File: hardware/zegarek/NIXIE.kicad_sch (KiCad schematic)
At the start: 32 parts, among them U6 74141, U7 74141, U8 74141, U9 74141

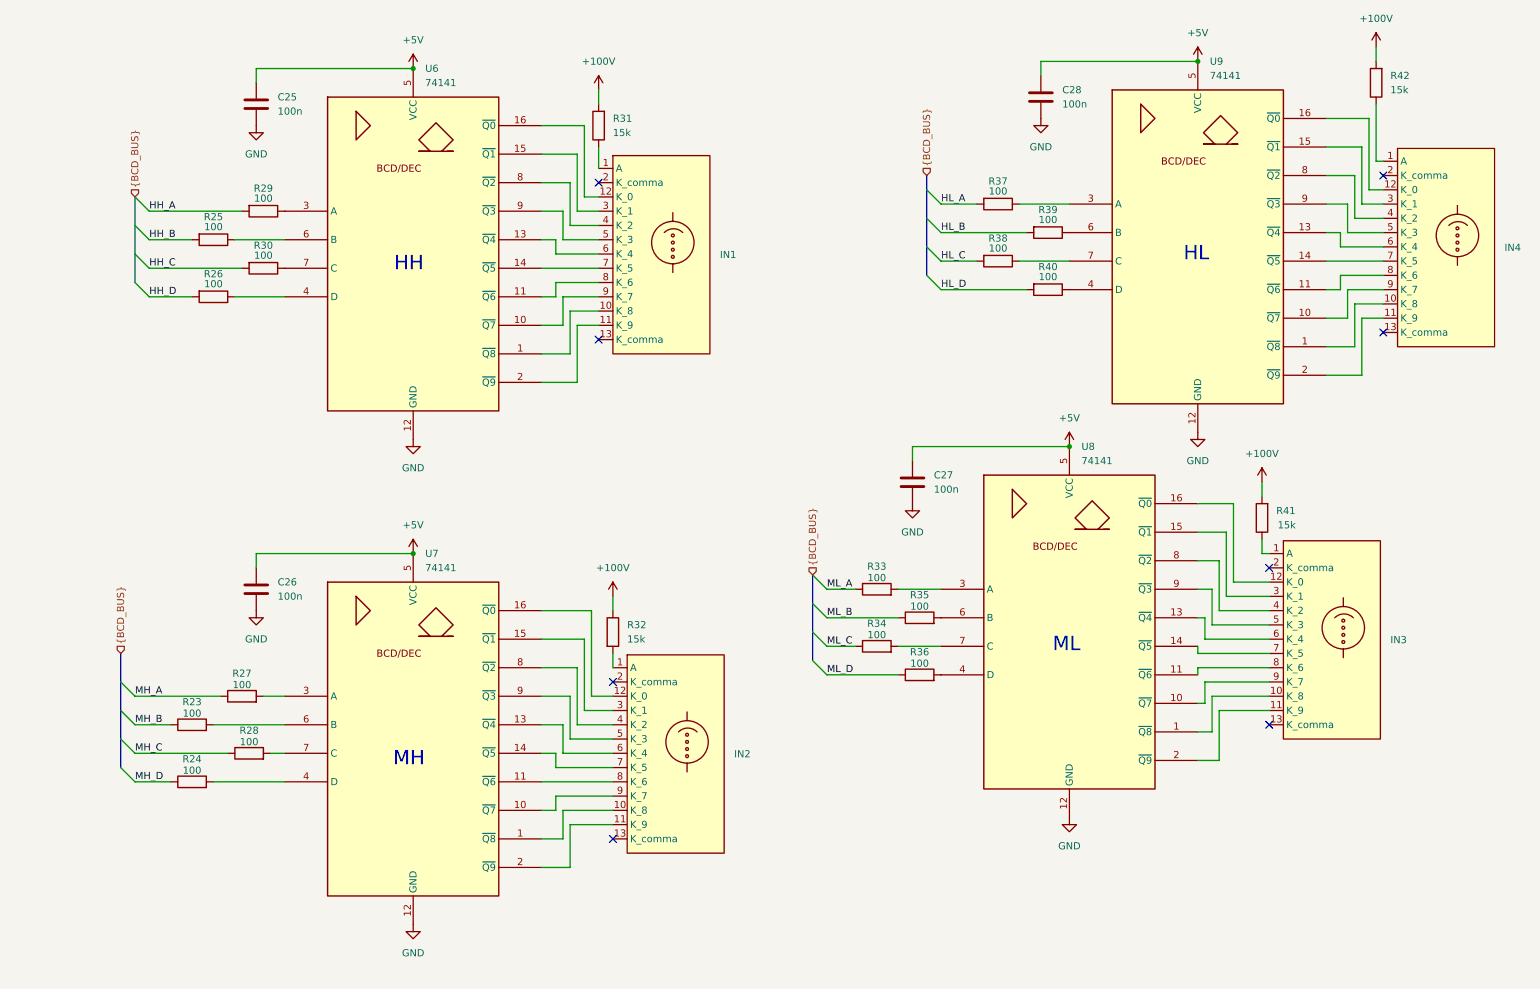
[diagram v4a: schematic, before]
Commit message: new revision with fixes from prototype: level shift to mcu added, changed con footprints and debug usb deleted
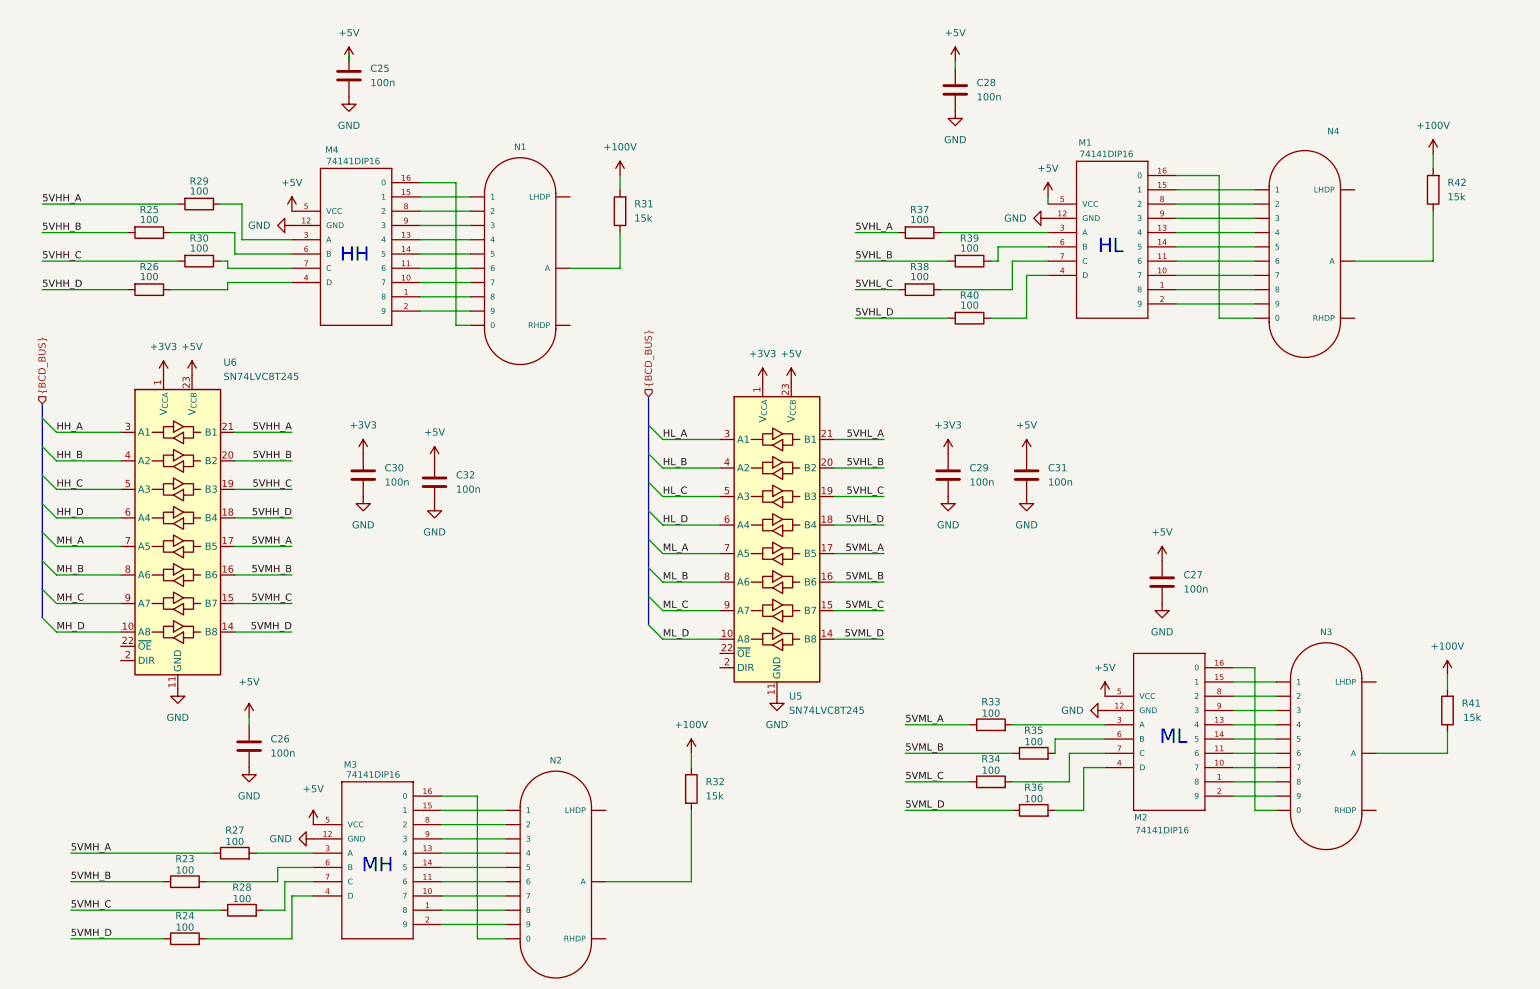
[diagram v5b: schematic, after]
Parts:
- removed IN1, IN2, IN3, IN4: (no value), Relay_THT:IN-14 NIXIE TUBE, symbol New_Library:IN-14
- removed U6, U7, U8, U9: 74141, Package_DIP:CERDIP-16_W7.62mm_SideBrazed_LongPads, symbol 74xx_IEEE:74141
- added C29, C30, C31, C32: 100n, Capacitor_SMD:C_1206_3216Metric_Pad1.33x1.80mm_HandSolder, symbol Device:C
- added M1, M2, M3, M4: 74141DIP16, nixiemisc:nixiemisc-DIP16, symbol nixiemisc:74141DIP16
- added N1, N2, N3, N4: IN-14, nixies-us:nixies-us-IN-14, symbol nixies-us:IN-14
- added U5, U6: SN74LVC8T245, Package_SO:SSOP-24_3.9x8.7mm_P0.635mm, symbol Logic_LevelTranslator:SN74LVC8T245
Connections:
- net +5V: now also C31.1, C32.1, M1.5 (VCC), M2.5 (VCC), M3.5 (VCC), M4.5 (VCC), U5.23 (V_{CCB}), U5.24 (V_{CCB}), U6.23 (V_{CCB}), U6.24 (V_{CCB})
- net GND: now also C29.2, C30.2, C31.2, C32.2, M1.12 (GND), M2.12 (GND), M3.12 (GND), M4.12 (GND), U5.11 (GND), U5.12 (GND), U5.13 (GND), U6.11 (GND), U6.12 (GND), U6.13 (GND)
- net HH_A: now also U6.3 (A1); no longer R29.2
- net HH_B: now also U6.4 (A2); no longer R25.2
- net HH_C: now also U6.5 (A3); no longer R30.2
- net HH_D: now also U6.6 (A4); no longer R26.2
- net HL_A: now also U5.3 (A1); no longer R37.2
- net HL_B: now also U5.4 (A2); no longer R39.2
- net HL_C: now also U5.5 (A3); no longer R38.2
- net HL_D: now also U5.6 (A4); no longer R40.2
- net MH_A: now also U6.7 (A5); no longer R27.1
- net MH_B: now also U6.8 (A6); no longer R23.1
- net MH_C: now also U6.9 (A7); no longer R28.1
- net MH_D: now also U6.10 (A8); no longer R24.1
- net ML_A: now also U5.7 (A5); no longer R33.1
- net ML_B: now also U5.8 (A6); no longer R35.1
- net ML_C: now also U5.9 (A7); no longer R34.1
- net ML_D: now also U5.10 (A8); no longer R36.1
- net at R40.1: now also M1.4 (D)
- net at R27.2: now also M3.3 (A)
- net at R24.2: now also M3.4 (D)
- net at R23.2: now also M3.6 (B)
- net at R28.2: now also M3.7 (C)
- net at R35.2: now also M2.6 (B)
- net at R29.1: now also M4.3 (A)
- net at R33.2: now also M2.3 (A)
- net at R38.1: now also M1.7 (C)
- net at R42.1: now also N4.A
- net at R36.2: now also M2.4 (D)
- net at R30.1: now also M4.7 (C)
- net at R37.1: now also M1.3 (A)
- net at R26.1: now also M4.4 (D)
- net at R25.1: now also M4.6 (B)
- net at R41.1: now also N3.A
- net at R31.1: now also N1.A
- net at R34.2: now also M2.7 (C)
- net at R39.1: now also M1.6 (B)
- net at R32.2: now also N2.A
- new net: M2.16 (0), N3.0
- new net: M2.15 (1), N3.1
- new net: M2.8 (2), N3.2
- new net: M2.9 (3), N3.3
- new net: M2.13 (4), N3.4
- new net: M2.14 (5), N3.5
- new net: M2.11 (6), N3.6
- new net: M2.10 (7), N3.7
- new net: M2.1 (8), N3.8
- new net: M2.2 (9), N3.9
- new net: M4.1 (8), N1.8
- new net: M4.10 (7), N1.7
- new net: M4.11 (6), N1.6
- new net: M4.13 (4), N1.4
- new net: M4.14 (5), N1.5
- new net: M4.15 (1), N1.1
- new net: M4.16 (0), N1.0
- new net: M4.2 (9), N1.9
- new net: M4.8 (2), N1.2
- new net: M4.9 (3), N1.3
- new net: M3.16 (0), N2.0
- new net: M3.15 (1), N2.1
- new net: M3.8 (2), N2.2
- new net: M3.9 (3), N2.3
- new net: M3.13 (4), N2.4
- new net: M3.14 (5), N2.5
- new net: M3.11 (6), N2.6
- new net: M3.10 (7), N2.7
- new net: M3.1 (8), N2.8
- new net: M3.2 (9), N2.9
- new net: M1.16 (0), N4.0
- new net: M1.15 (1), N4.1
- new net: M1.8 (2), N4.2
- new net: M1.9 (3), N4.3
- new net: M1.13 (4), N4.4
- new net: M1.14 (5), N4.5
- new net: M1.11 (6), N4.6
- new net: M1.10 (7), N4.7
- new net: M1.1 (8), N4.8
- new net: M1.2 (9), N4.9
- new net +3V3: C29.1, C30.1, U5.1 (V_{CCA}), U6.1 (V_{CCA})
- new net 5VHH_A: R29.2, U6.21 (B1)
- new net 5VHH_B: R25.2, U6.20 (B2)
- new net 5VHH_C: R30.2, U6.19 (B3)
- new net 5VHH_D: R26.2, U6.18 (B4)
- new net 5VHL_A: R37.2, U5.21 (B1)
- new net 5VHL_B: R39.2, U5.20 (B2)
- new net 5VHL_C: R38.2, U5.19 (B3)
- new net 5VHL_D: R40.2, U5.18 (B4)
- new net 5VMH_A: R27.1, U6.17 (B5)
- new net 5VMH_B: R23.1, U6.16 (B6)
- new net 5VMH_C: R28.1, U6.15 (B7)
- new net 5VMH_D: R24.1, U6.14 (B8)
- new net 5VML_A: R33.1, U5.17 (B5)
- new net 5VML_B: R35.1, U5.16 (B6)
- new net 5VML_C: R34.1, U5.15 (B7)
- new net 5VML_D: R36.1, U5.14 (B8)
- no-connect marks 8 -> 0
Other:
- moved on the sheet: C25, C26, C27, C28, R23, R24, R25, R26, R27, R28, R29, R30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

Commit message: rerouting tubes order for proper display order
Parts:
- R40: footprint Resistor_SMD:R_1206_3216Metric_Pad1.30x1.75mm_HandSolder -> Resistor_SMD:R_0603_1608Metric_Pad0.98x0.95mm_HandSolder
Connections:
- net 5VHH_A: now also U5.21 (B1); no longer U6.21 (B1)
- net 5VHH_B: now also U5.20 (B2); no longer U6.20 (B2)
- net 5VHH_C: now also U5.19 (B3); no longer U6.19 (B3)
- net 5VHH_D: now also U5.18 (B4); no longer U6.18 (B4)
- net 5VHL_A: now also U5.17 (B5); no longer U5.21 (B1)
- net 5VHL_B: now also U5.16 (B6); no longer U5.20 (B2)
- net 5VHL_C: now also U5.15 (B7); no longer U5.19 (B3)
- net 5VHL_D: now also U5.14 (B8); no longer U5.18 (B4)
- net 5VMH_A: now also U6.21 (B1); no longer U6.17 (B5)
- net 5VMH_B: now also U6.20 (B2); no longer U6.16 (B6)
- net 5VMH_C: now also U6.19 (B3); no longer U6.15 (B7)
- net 5VMH_D: now also U6.18 (B4); no longer U6.14 (B8)
- net 5VML_A: now also U6.17 (B5); no longer U5.17 (B5)
- net 5VML_B: now also U6.16 (B6); no longer U5.16 (B6)
- net 5VML_C: now also U6.15 (B7); no longer U5.15 (B7)
- net 5VML_D: now also U6.14 (B8); no longer U5.14 (B8)
- net HH_A: now also U5.3 (A1); no longer U6.3 (A1)
- net HH_B: now also U5.4 (A2); no longer U6.4 (A2)
- net HH_C: now also U5.5 (A3); no longer U6.5 (A3)
- net HH_D: now also U5.6 (A4); no longer U6.6 (A4)
- net HL_A: now also U5.7 (A5); no longer U5.3 (A1)
- net HL_B: now also U5.8 (A6); no longer U5.4 (A2)
- net HL_C: now also U5.9 (A7); no longer U5.5 (A3)
- net HL_D: now also U5.10 (A8); no longer U5.6 (A4)
- net MH_A: now also U6.3 (A1); no longer U6.7 (A5)
- net MH_B: now also U6.4 (A2); no longer U6.8 (A6)
- net MH_C: now also U6.5 (A3); no longer U6.9 (A7)
- net MH_D: now also U6.6 (A4); no longer U6.10 (A8)
- net ML_A: now also U6.7 (A5); no longer U5.7 (A5)
- net ML_B: now also U6.8 (A6); no longer U5.8 (A6)
- net ML_C: now also U6.9 (A7); no longer U5.9 (A7)
- net ML_D: now also U6.10 (A8); no longer U5.10 (A8)

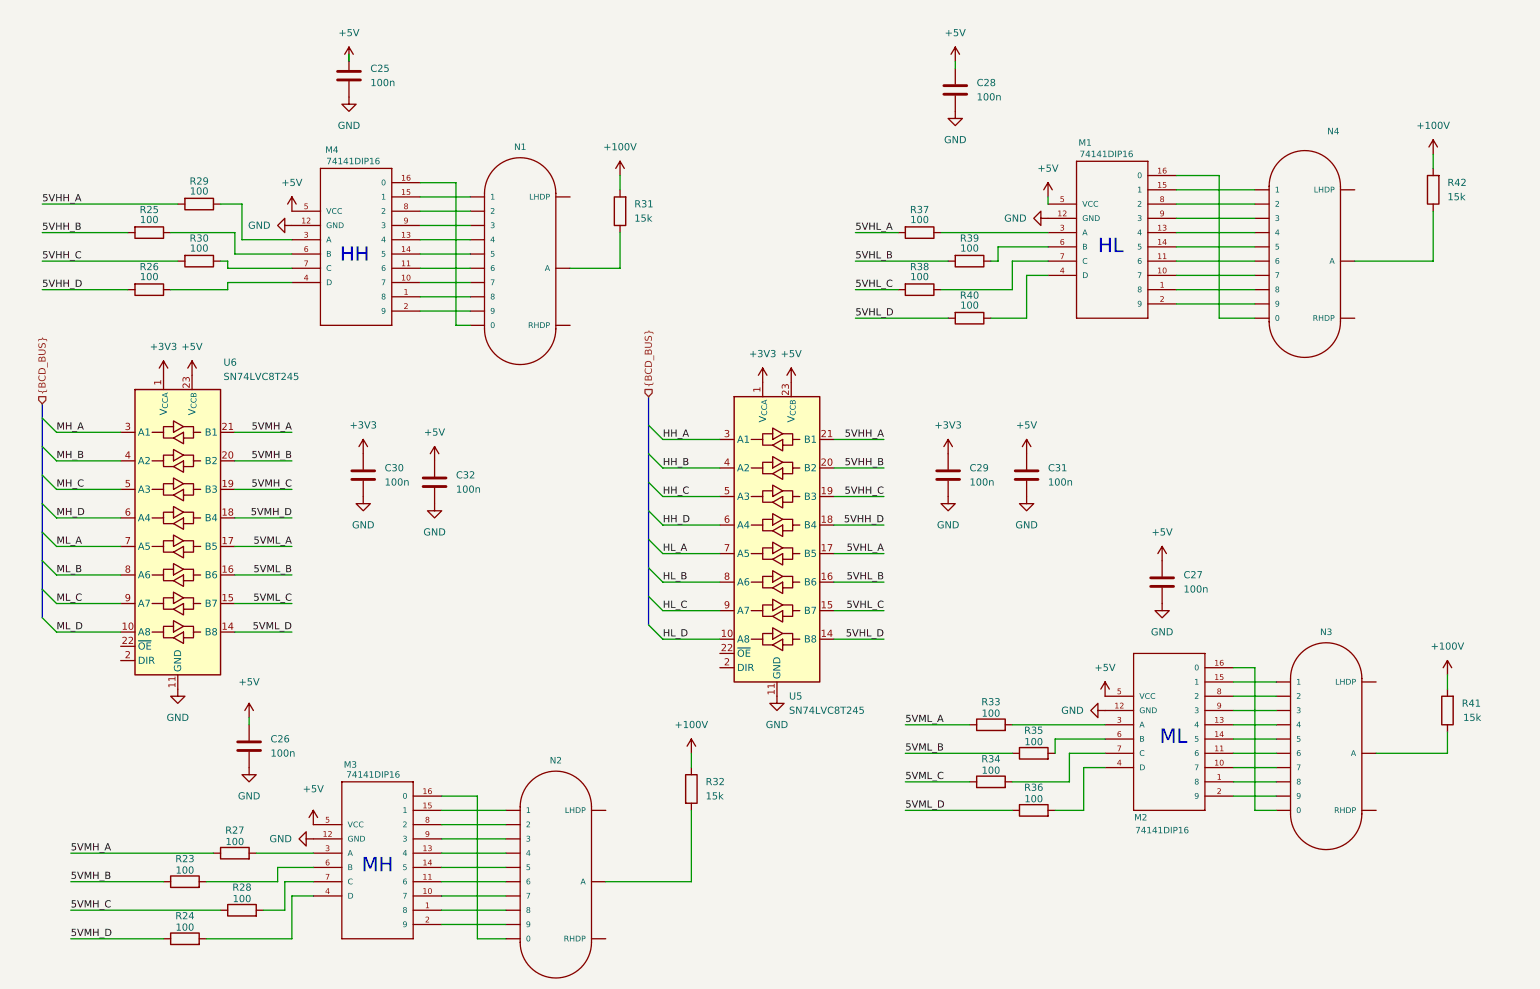
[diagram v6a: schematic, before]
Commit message: correction changes, postprod files regenration,added OE and EN to MCU schematic
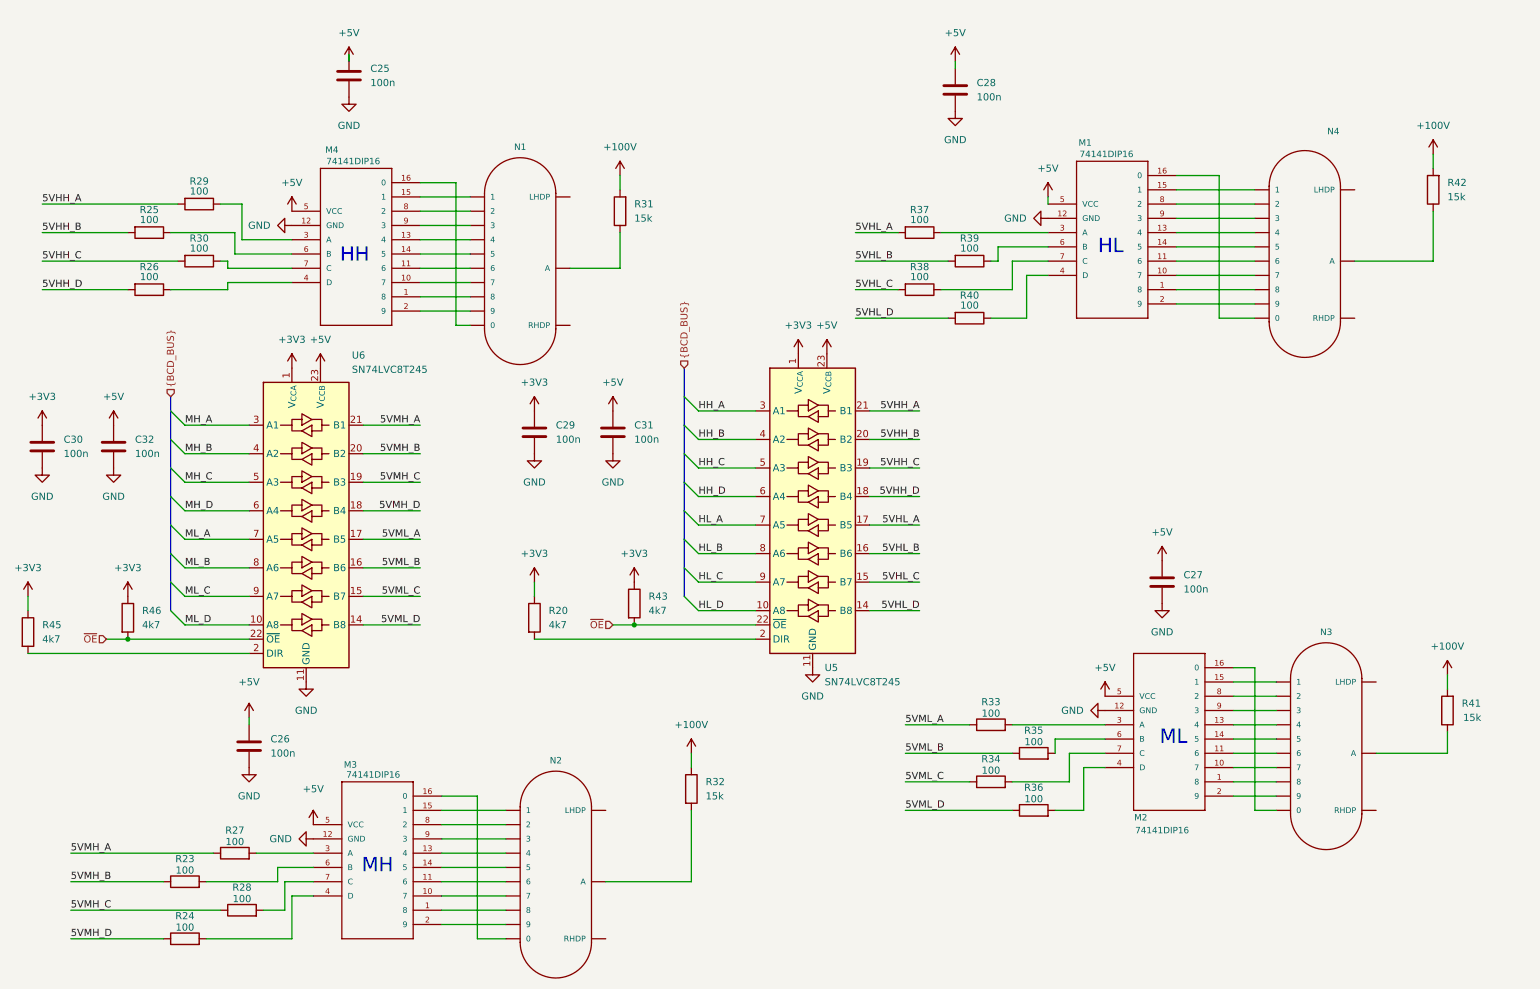
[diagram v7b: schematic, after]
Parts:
- added R20, R43, R45, R46: 4k7, symbol Device:R
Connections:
- net +3V3: now also R20.1, R43.1, R45.1, R46.1
- net at U5.2 (DIR): now also R20.2
- net ~{OE}: now reaches U5.22 (~{OE})
- net ~{OE}: now also U6.22 (~{OE}), R43.2, R46.2
- net at U6.2 (DIR): now also R45.2
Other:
- moved on the sheet: C29, C30, C31, C32, U5, U6

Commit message: reqenerating postprod
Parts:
- removed R20, R45: 4k7, symbol Device:R
- added RN1, RN2: 10k, Resistor_SMD:R_Array_Convex_2x0606, symbol Device:R_Pack02
- R31, R32, R41, R42: value 15k -> 56k; footprint Resistor_SMD:R_0603_1608Metric_Pad0.98x0.95mm_HandSolder -> Resistor_SMD:R_1206_3216Metric_Pad1.30x1.75mm_HandSolder
- R43, R46: value 4k7 -> 10k; footprint (none) -> Resistor_SMD:R_0603_1608Metric_Pad0.98x0.95mm_HandSolder
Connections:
- net +3V3: now also RN1.1 (R1.1), RN2.1 (R1.1)
- net GND: now also RN1.2 (R2.1), RN2.2 (R2.1)
- net at U5.2 (DIR): now also RN2.3 (R2.2), RN2.4 (R1.2)
- net at U6.2 (DIR): now also RN1.3 (R2.2), RN1.4 (R1.2)
- net ~{OE} renamed HOUR_~{OE}
- net HOUR_~{OE}: no longer R46.2, U6.22 (~{OE})
- new net MIN_~{OE}: R46.2, U6.22 (~{OE})
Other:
- moved on the sheet: C25, C26, C27, C28, C29, C30, C31, C32, M1, M4, N1, N4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
